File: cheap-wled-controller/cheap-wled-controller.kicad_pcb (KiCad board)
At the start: 2 copper layers, 98 x 48 mm, 47 parts, among them J10 Conn_01x05_Pin, J2 USB_C_Receptacle, J4 Conn_02x05_Odd_Even, J6 Conn_01x05_Pin, J7 Conn_01x02_Pin, J8 Conn_01x07_Pin, SW1 SW_Push, U1 USBLC6-2SC6, U3 CH224K, U4 MX5014S, U5 ESP32-S3-WROOM-1-N4R2, U7 TPS54202DDC, U9 AMS1117-3.3

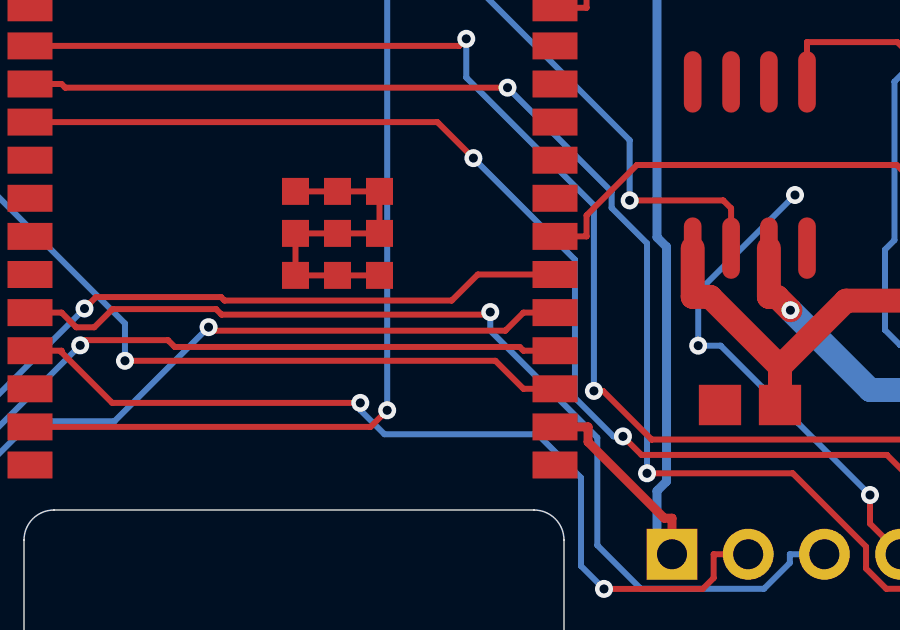
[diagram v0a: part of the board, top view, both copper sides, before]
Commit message: added some GND for the esp32
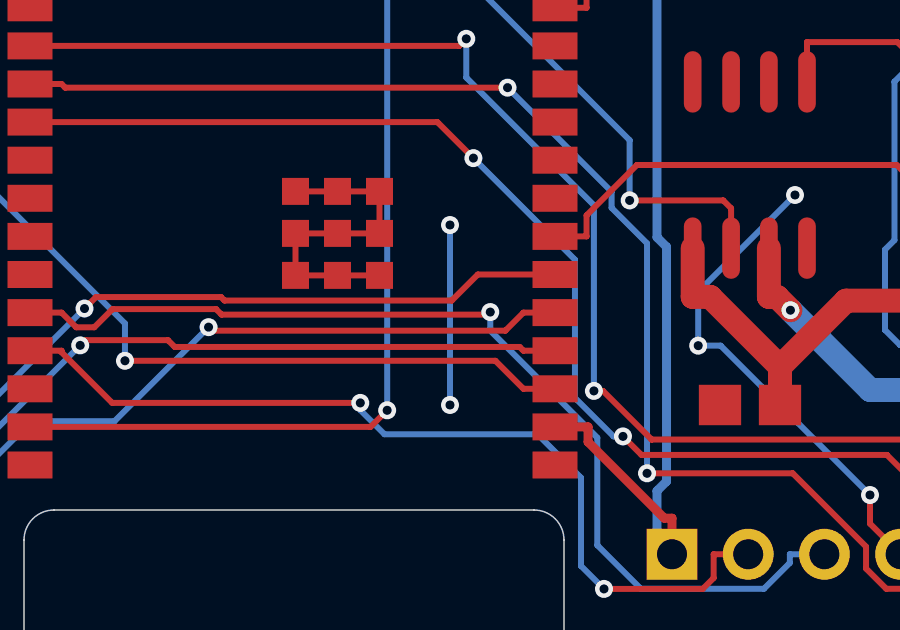
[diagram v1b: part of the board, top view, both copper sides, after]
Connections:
- U5 pad 1: unconnected-(U5-GND-Pad1) -> GND
- U5 pad 41: unconnected-(U5-EPAD-Pad41) -> GND
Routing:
- net GND: track 19.8 -> 37.0 mm, vias 7 -> 9
- net unconnected-(U5-EPAD-Pad41): track 11.2 -> 0.00 mm

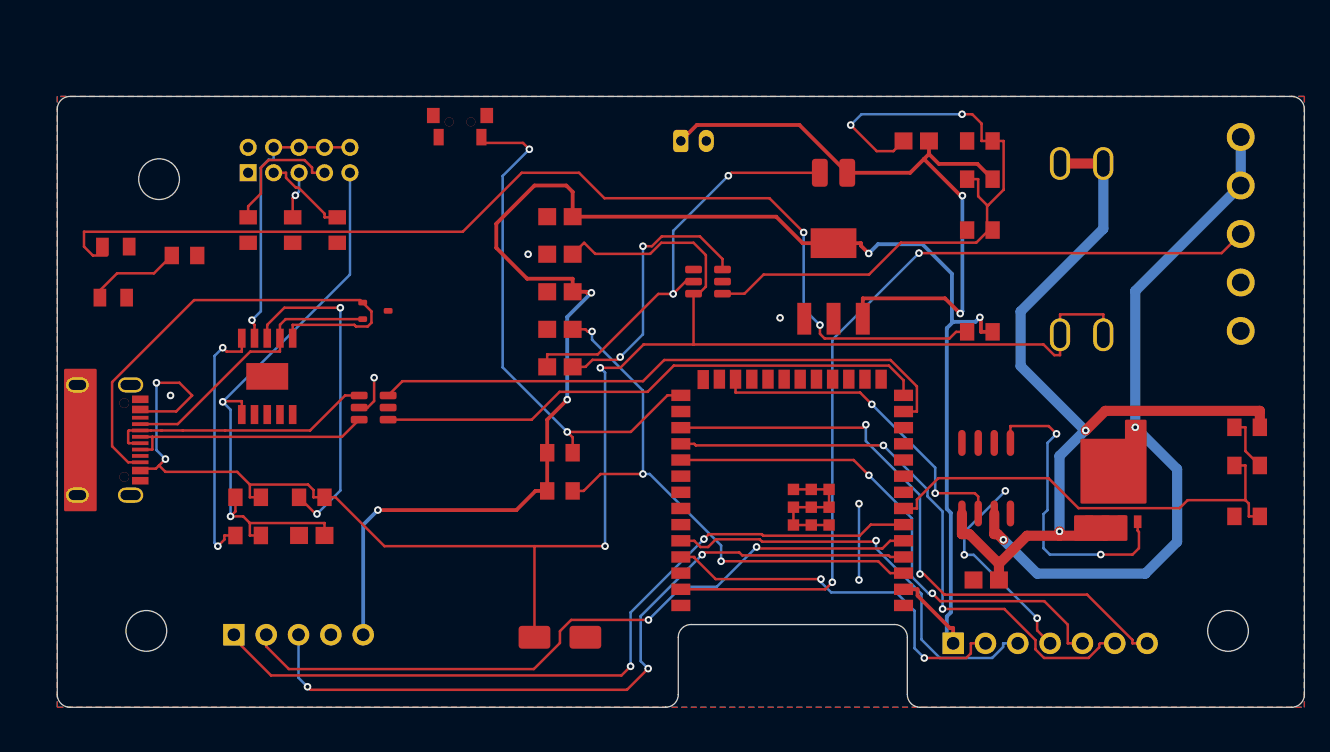
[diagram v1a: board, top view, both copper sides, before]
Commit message: right position for the holes
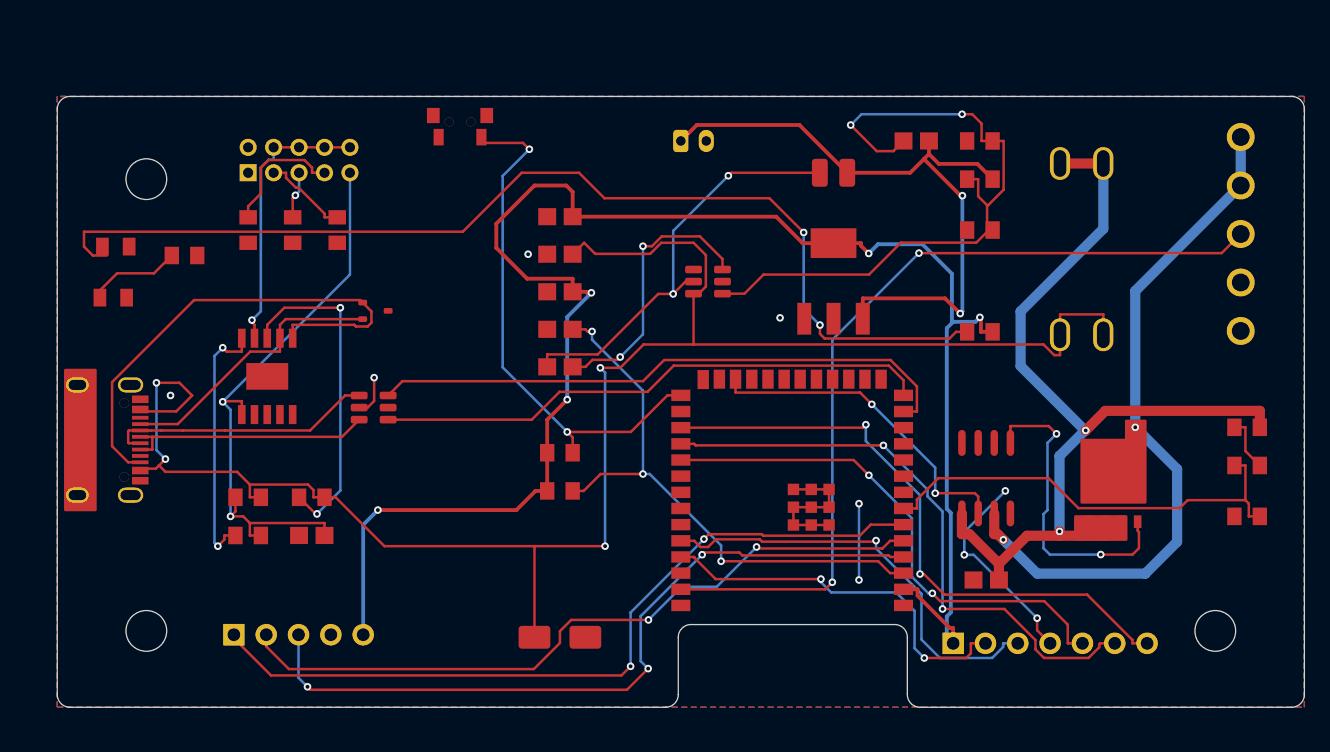
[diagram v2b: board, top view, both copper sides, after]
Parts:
- moved H1 1.00 mm to (19.0, 18.5)
- moved H3 1.00 mm to (103.0, 54.0)
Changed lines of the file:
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@@
 	(footprint "MountingHole:MountingHole_3.2mm_M3"
 		(layer "F.Cu")
-		(at 20 18.5)
+		(at 19 18.5)
 		(descr "Mounting Hole 3.2mm, no annular, M3")
 		(tags "mounting hole 3.2mm no annular m3")
@@
 	(footprint "MountingHole:MountingHole_3.2mm_M3"
 		(layer "F.Cu")
-		(at 104 54)
+		(at 103 54)
 		(descr "Mounting Hole 3.2mm, no annular, M3")
 		(tags "mounting hole 3.2mm no annular m3")

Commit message: new design mini 5x5
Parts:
- removed D4: LED_Small, cheap-wled-controller:LED0805-R-RD
- removed F2: DIR, cheap-wled-controller:FUSE-TH_XF-508P-A-B
- removed H1: ~, MountingHole:MountingHole_3.2mm_M3
- removed R12: 10k, cheap-wled-controller:R0805
- removed REF**: DFN-8_L5.9-W5.2-P1.27-LS6.2-BL, cheap-wled-controller:DFN-8_L5.9-W5.2-P1.27-LS6.2-BL
- added C4: 10u, cheap-wled-controller:C0805, F.Cu at (48.2, 44.6)
- added C8: 10u, cheap-wled-controller:C0805, F.Cu at (48.2, 38.7)
- added C9: 1u, cheap-wled-controller:C0805, F.Cu at (48.2, 41.7)
- added Q3: NMOS, cheap-wled-controller:DFN-8_L5.9-W5.2-P1.27-LS6.2-BL, F.Cu at (50.3, 51.4)
- D3, U9: moved to B.Cu
- moved H3 87.0 mm to (16.0, 56.0)
- moved R11 82.6 mm to (23.5, 35.0)
- moved R10 77.7 mm to (28.0, 35.0)
- moved R15 73.1 mm to (32.5, 35.0), turned to 180 degrees
- moved R14 71.0 mm to (15.0, 45.0)
- moved J8 58.7 mm to (23.8, 57.5)
- moved H2 53.0 mm to (56.0, 16.0)
- moved J10 51.4 mm to (55.5, 36.5)
- moved C1 50.8 mm to (34.2, 49.1)
- moved R22 50.8 mm to (43.5, 45.5)
- moved C30 47.0 mm to (38.5, 38.4)
- moved U9 46.5 mm to (31.2, 46.8)
- moved R13 45.8 mm to (43.5, 43.0)
- moved U4 44.3 mm to (41.5, 50.5), turned to -90 degrees
- moved L2 42.2 mm to (38.6, 42.4)
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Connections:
- C1 pad 2: /V_LED -> /VBUS_C
- J2 pad 0: Earth -> GND
- J2 pad 1: Earth -> GND
- J2 pad 2: Earth -> GND
- J2 pad 3: Earth -> GND
- R15 pad 2: /V_LED -> /VBUS_C
- U3 pad 11: (no net) -> GND
- U4 pad 1: /V_LED -> /VBUS_C
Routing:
- net Net-(D2-A): track 84.1 -> 3.04 mm, vias 2 -> 0
- net /V_LED: track 71.1 -> 0.00 mm, vias 2 -> 0
- net /LED_1_VCC: track 54.9 -> 0.00 mm, vias 2 -> 0
- net GND: track 37.0 -> 81.0 mm, vias 9 -> 22
- net Net-(D1-K1): track 39.5 -> 78.2 mm, vias 0 -> 5
- net /LED_DATA: track 66.7 -> 30.2 mm
- net Net-(D1-K2): track 22.1 -> 49.7 mm, vias 0 -> 3
- net /FB: track 53.5 -> 26.9 mm
- net /TX: track 30.1 -> 53.0 mm, vias 2 -> 3
- net /D-_OUT: track 46.6 -> 27.5 mm, vias 0 -> 2
- net Net-(U3-PG): track 20.6 -> 3.33 mm, vias 2 -> 0
- net Net-(U5-EN): track 45.0 -> 29.0 mm, vias 3 -> 0
- net /SW_5V: track 33.2 -> 17.9 mm, vias 2 -> 0
- net /BOOT: track 21.6 -> 6.40 mm, vias 2 -> 0
- net /GPIO6: track 62.3 -> 47.2 mm, vias 2 -> 7
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- added copper zone on F.Cu, net /LED_1_VCC
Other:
- board size 98 x 48 mm -> 48 x 48 mm

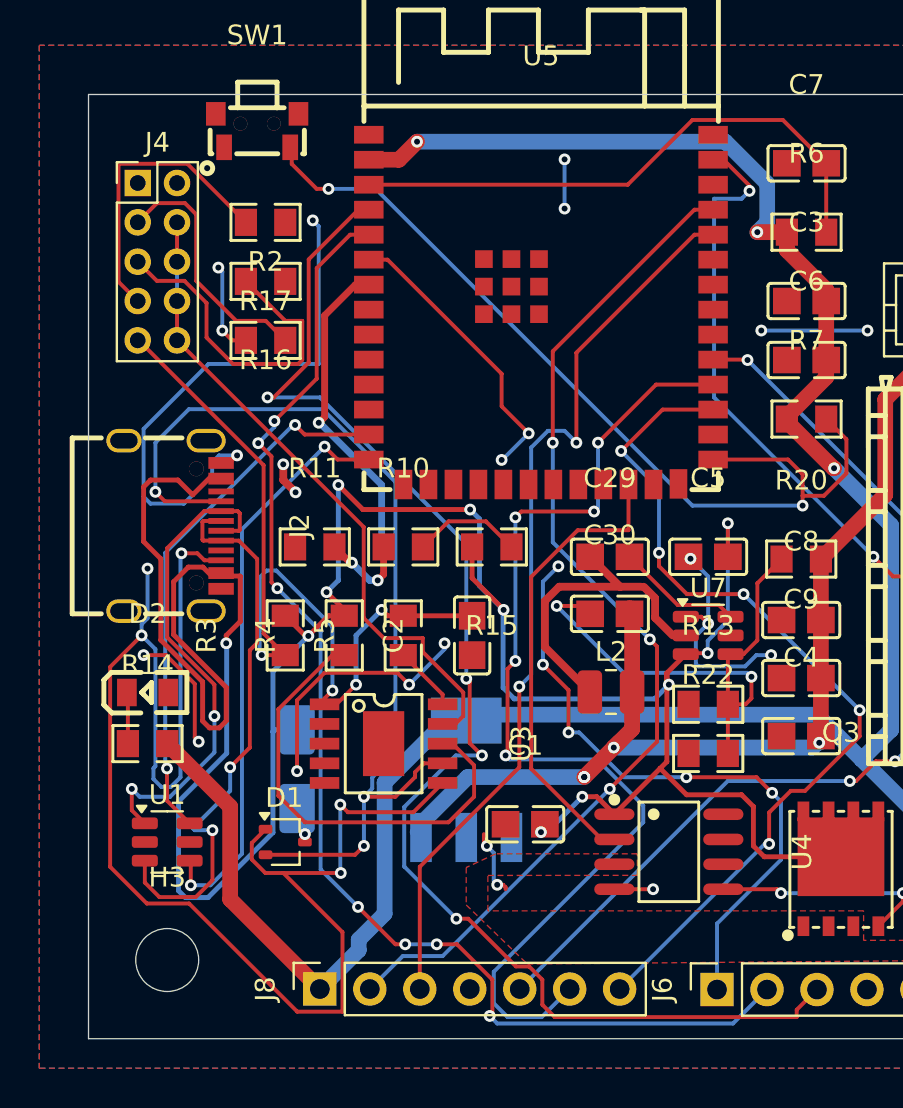
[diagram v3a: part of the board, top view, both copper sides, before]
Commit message: all tracks connected
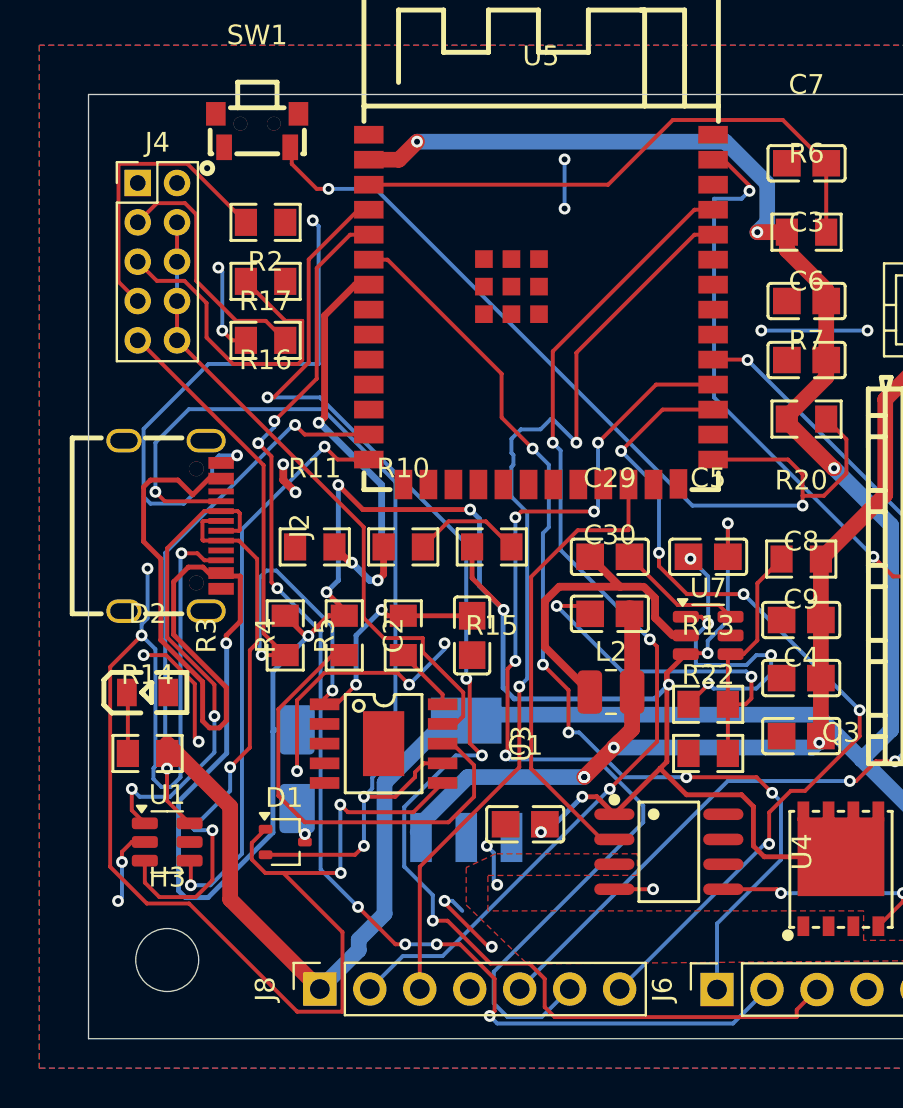
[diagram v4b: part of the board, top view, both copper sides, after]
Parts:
- moved R14 0.50 mm to (15.0, 45.5)
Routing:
- net GND: track 81.0 -> 94.2 mm, vias 22 -> 27
- net /GPIO6: track 47.2 -> 52.2 mm, vias 7 -> 5
- net /RX: track 46.8 -> 48.9 mm
- net /GPIO4: track 70.2 -> 71.1 mm

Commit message: drc
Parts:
- moved R14 0.50 mm to (15.0, 45.0)
- moved SW1 0.30 mm to (20.6, 14.1)
- moved C1 0.20 mm to (34.2, 48.9)
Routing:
- net /VBUS_C: track 144.8 -> 141.2 mm
- net /VOLT_OUT: track 20.9 -> 22.5 mm
- net Net-(U5-IO0): track 46.8 -> 45.5 mm
- net Net-(J4-Pin_7): track 15.1 -> 15.9 mm
- net /VDD_C: track 44.5 -> 45.2 mm

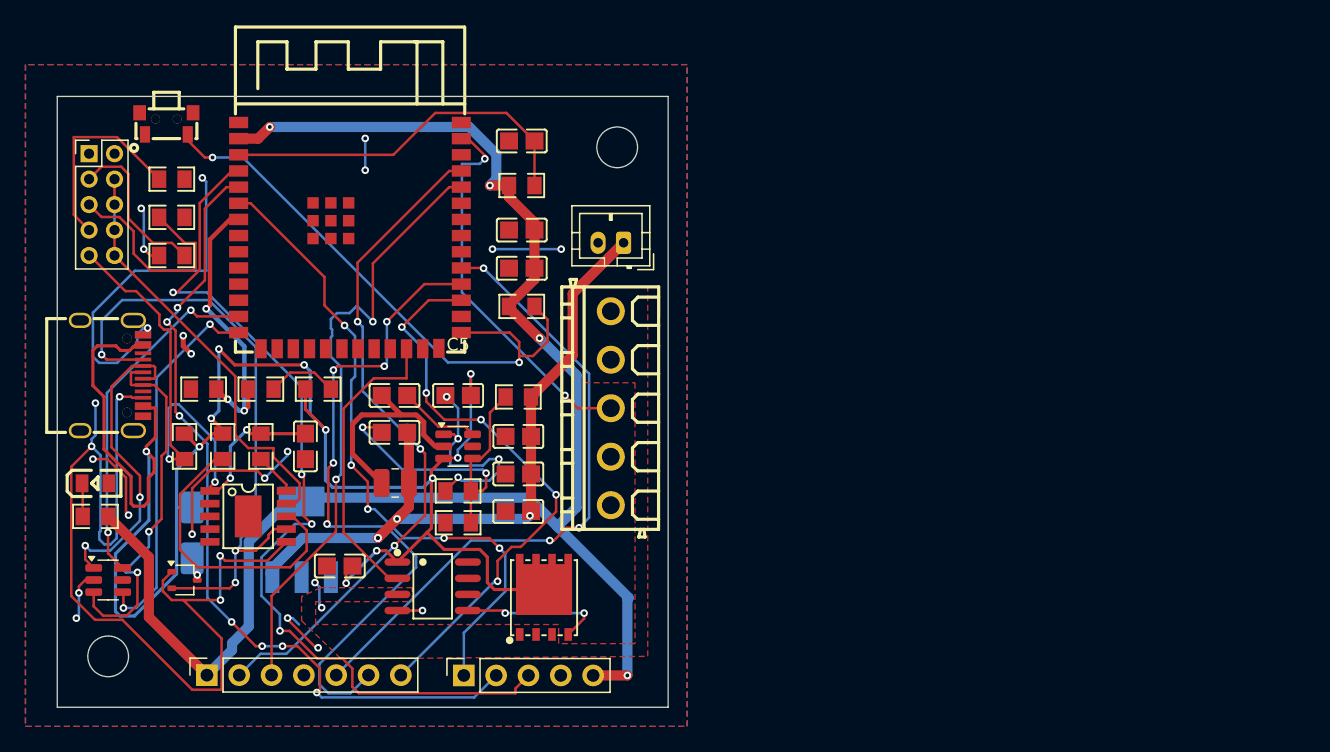
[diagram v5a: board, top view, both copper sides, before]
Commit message: added capacitors for ams1117 and TSOP38238
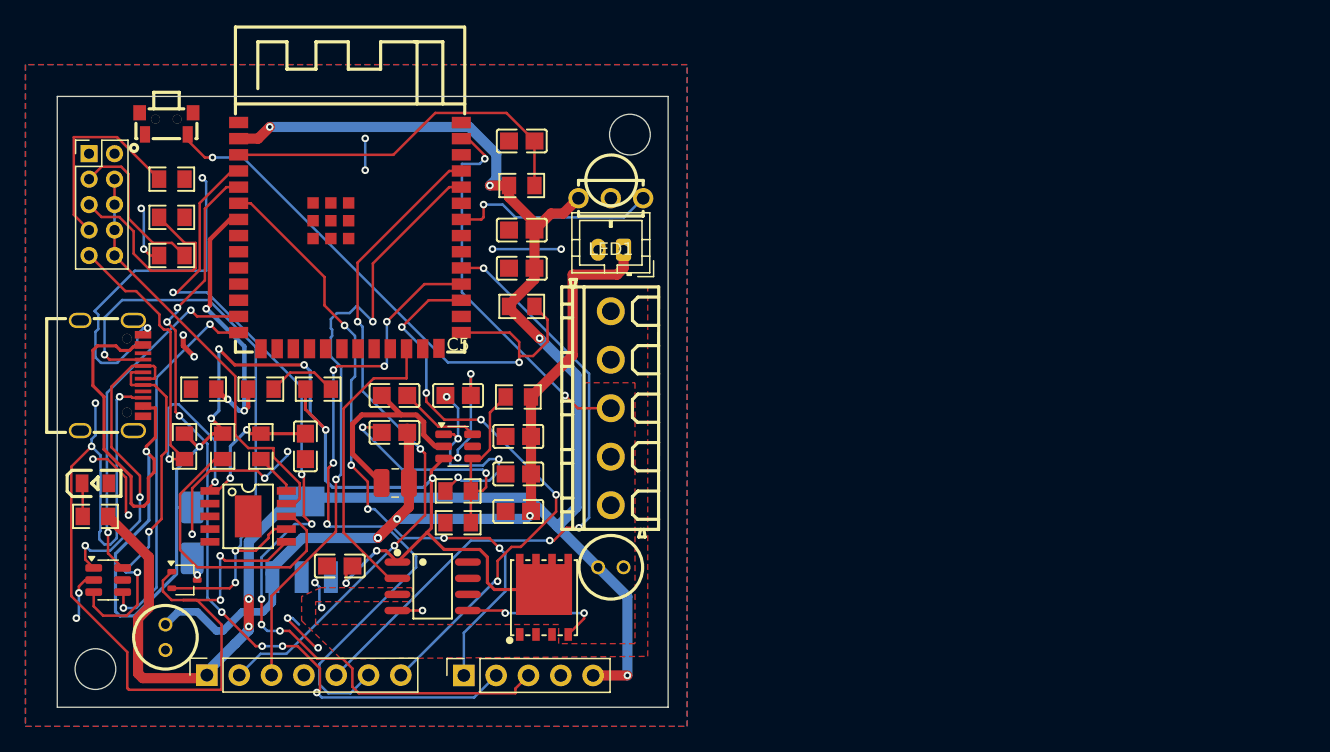
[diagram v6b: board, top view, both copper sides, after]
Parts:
- added C10: 50YXJ22M5X11, cheap-wled-controller:CAP-TH_BD5.0-P2.00-D0.5-FD-1, F.Cu at (55.5, 49.0)
- added C11: 50YXJ22M5X11, cheap-wled-controller:CAP-TH_BD5.0-P2.00-D0.5-FD-1, F.Cu at (20.5, 54.5)
- added LED1: TSOP38238, cheap-wled-controller:SENSOR-TG_TSOP38236, F.Cu at (55.5, 20.0)
- moved H2 1.41 mm to (57.0, 15.0)
- moved H3 1.41 mm to (15.0, 57.0)
- moved J7 0.55 mm to (56.5, 24.1)
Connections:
- U3 pad 11: GND -> (no net)
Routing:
- net /GPIO41: track 0.00 -> 16.4 mm, vias 0 -> 1
- net +5V: track 55.5 -> 69.3 mm
- net +3.3V: track 127.9 -> 136.3 mm, vias 4 -> 6
- net Net-(D1-K1): track 77.7 -> 80.0 mm
- net /GPIO4: track 71.1 -> 71.6 mm, vias 4 -> 6

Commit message: fixes
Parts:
- moved R13 0.30 mm to (43.5, 43.3)
- moved C11 0.22 mm to (20.7, 54.4)
- moved C10 0.10 mm to (55.6, 49.0), turned to 90 degrees
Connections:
- U3 pad 11: (no net) -> GND
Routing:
- net GND: track 94.2 -> 96.1 mm, vias 27 -> 26
- net +5V: track 69.3 -> 70.9 mm
- net Net-(D1-K2): track 49.3 -> 49.8 mm
- net +3.3V: track 136.3 -> 136.4 mm, vias 6 -> 5
